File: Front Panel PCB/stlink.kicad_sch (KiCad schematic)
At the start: 22 parts, among them J3 LCD I2C, J4 Fan Tach and PWM, J5 Fan Power and GND, J6 VP and VN, J7 DEBUG, Q21 2N3904, SW1 SW_Push, U12 STM32G031K8Tx

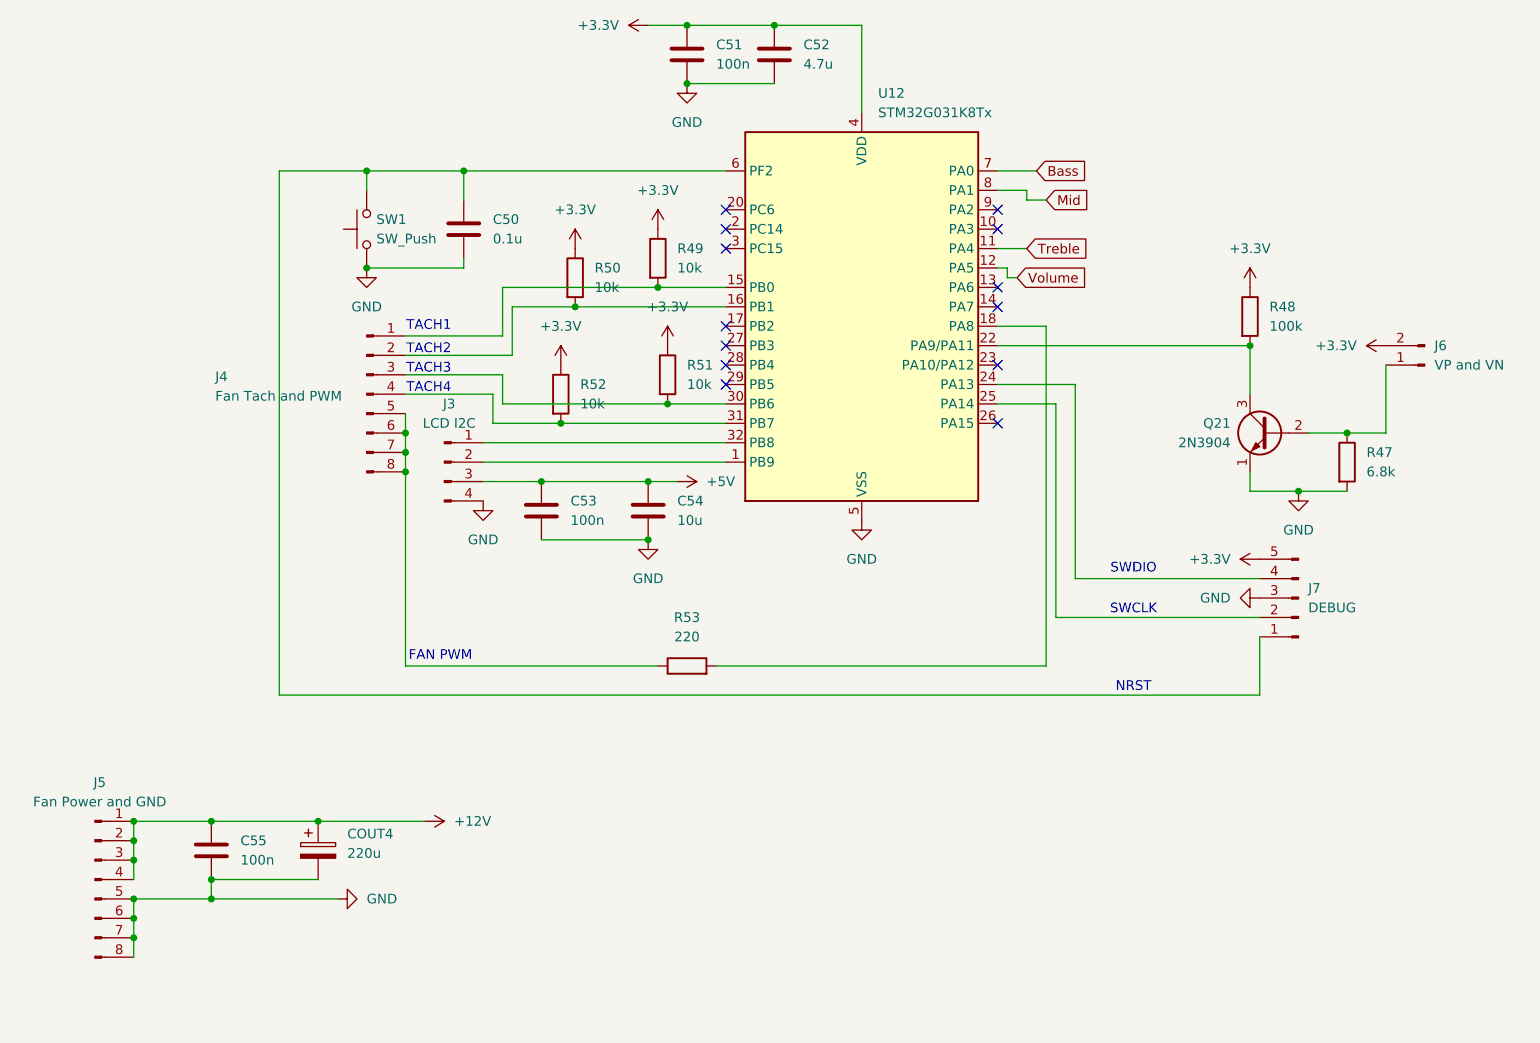
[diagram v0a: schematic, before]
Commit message: Checked ERC, assigned all footprints, time to start PCB design, will start with the equiliser
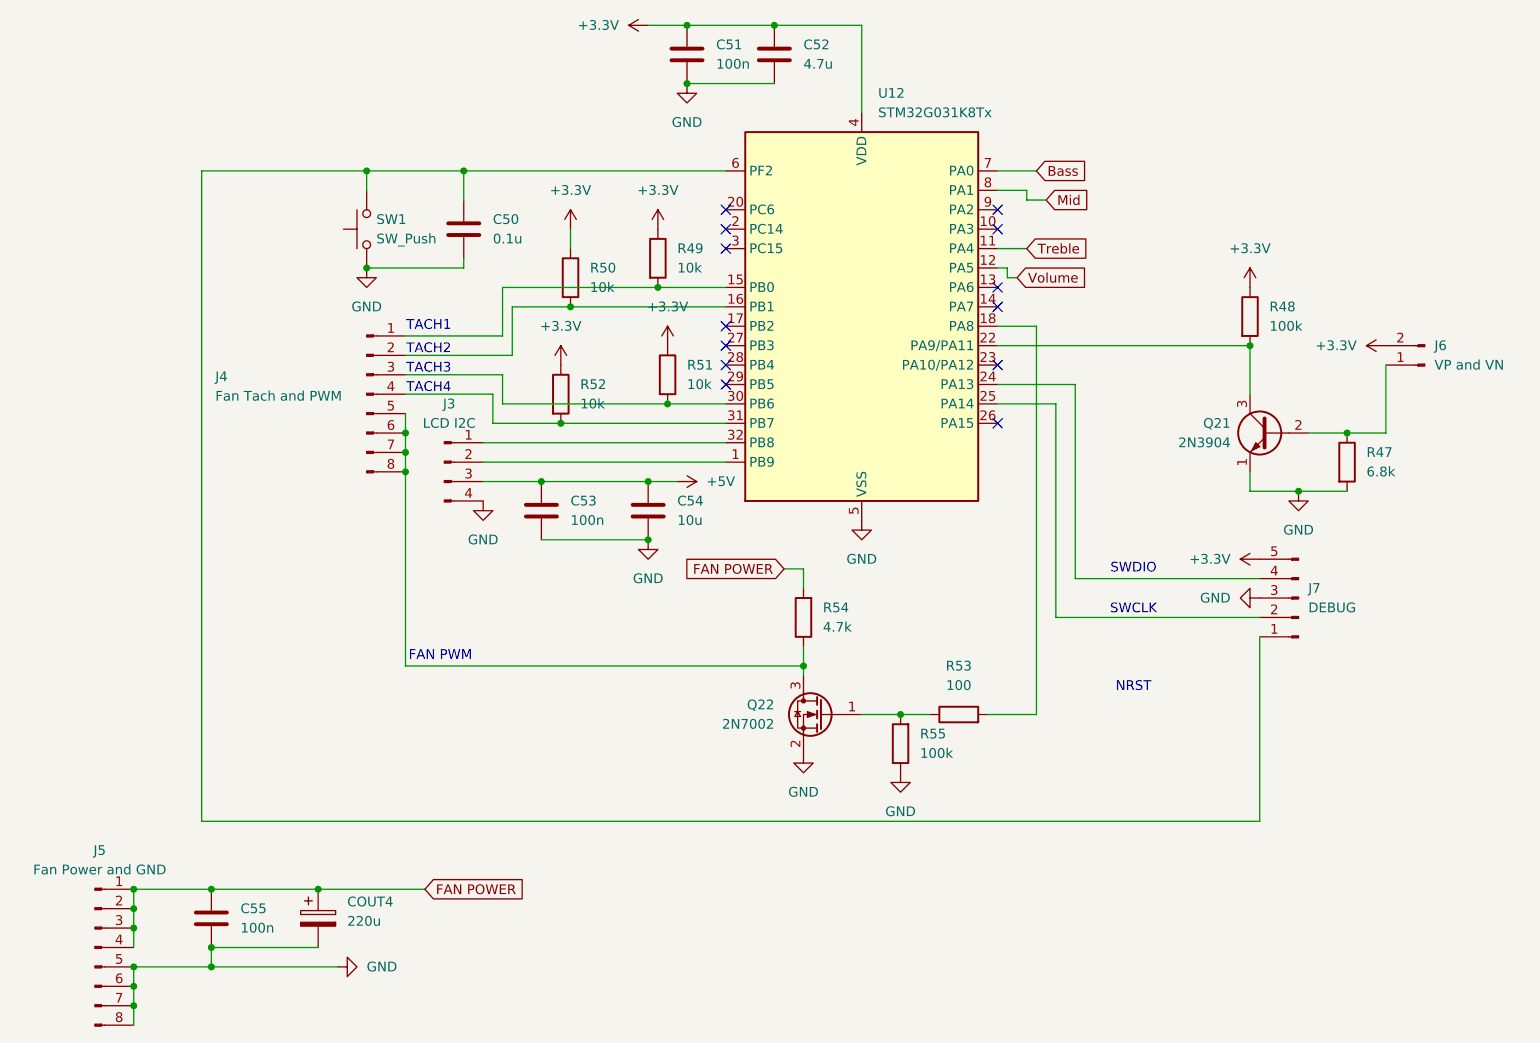
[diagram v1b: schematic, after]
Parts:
- added Q22: 2N7002, Package_TO_SOT_SMD:SOT-23, symbol Transistor_FET:2N7002
- added R54: 4.7k, Resistor_THT:R_Axial_DIN0207_L6.3mm_D2.5mm_P10.16mm_Horizontal, symbol Device:R
- added R55: 100k, Resistor_THT:R_Axial_DIN0207_L6.3mm_D2.5mm_P10.16mm_Horizontal, symbol Device:R
- C50, C51, C53, C55: footprint (none) -> Capacitor_THT:C_Rect_L7.2mm_W2.5mm_P5.00mm
- C52: footprint (none) -> GCJ31CC71H475KA01L:CAPC3216X190N
- C54: footprint (none) -> GCM32EC71H106KA03L:CAP_GCM32_MUR
- COUT4: footprint (none) -> Capacitor_THT:CP_Radial_D6.3mm_P2.50mm
- J3: footprint (none) -> Connector_PinHeader_2.00mm:PinHeader_1x04_P2.00mm_Vertical
- J4: footprint (none) -> Connector_JST:JST_XH_B8B-XH-A_1x08_P2.50mm_Vertical
- J5: footprint (none) -> Connector_Molex:Molex_Micro-Fit_3.0_43045-0812_2x04_P3.00mm_Vertical
- J6: footprint (none) -> Connector_JST:JST_PH_B2B-PH-K_1x02_P2.00mm_Vertical
- J7: footprint (none) -> Connector_JST:JST_PH_B5B-PH-K_1x05_P2.00mm_Vertical
- R47, R48, R49, R50, R51, R52: footprint (none) -> Resistor_THT:R_Axial_DIN0207_L6.3mm_D2.5mm_P10.16mm_Horizontal
- R53: value 220 -> 100; footprint (none) -> Resistor_THT:R_Axial_DIN0207_L6.3mm_D2.5mm_P10.16mm_Horizontal
- SW1: footprint (none) -> Button_Switch_THT:SW_PUSH_6mm_H5mm
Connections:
- net GND: now also Q22.2 (S), R55.1
- net at J4.5 (Pin_5), J4.6 (Pin_6), J4.7 (Pin_7)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: now also Q22.3 (D), R54.1; no longer R53.1
- net +12V renamed FAN POWER
- net FAN POWER: now also R54.2
- new net: Q22.1 (G), R53.1, R55.2
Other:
- moved on the sheet: C55, COUT4, J5, R50

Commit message: Hierarichal sheets and started PCB design
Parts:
- removed C50: 0.1u, Capacitor_THT:C_Rect_L7.2mm_W2.5mm_P5.00mm, symbol Device:C
- removed C51, C53, C55: 100n, Capacitor_THT:C_Rect_L7.2mm_W2.5mm_P5.00mm, symbol Device:C
- removed C52: 4.7u, GCJ31CC71H475KA01L:CAPC3216X190N, symbol Device:C
- removed C54: 10u, GCM32EC71H106KA03L:CAP_GCM32_MUR, symbol Device:C
- removed COUT4: 220u, Capacitor_THT:CP_Radial_D6.3mm_P2.50mm, symbol Device:C_Polarized
- removed J3: LCD I2C, Connector_PinHeader_2.00mm:PinHeader_1x04_P2.00mm_Vertical, symbol Connector:Conn_01x04_Pin
- removed J4: Fan Tach and PWM, Connector_JST:JST_XH_B8B-XH-A_1x08_P2.50mm_Vertical, symbol Connector:Conn_01x08_Pin
- removed J5: Fan Power and GND, Connector_Molex:Molex_Micro-Fit_3.0_43045-0812_2x04_P3.00mm_Vertical, symbol Connector:Conn_01x08_Pin
- removed J6: VP and VN, Connector_JST:JST_PH_B2B-PH-K_1x02_P2.00mm_Vertical, symbol Connector:Conn_01x02_Pin
- removed J7: DEBUG, Connector_JST:JST_PH_B5B-PH-K_1x05_P2.00mm_Vertical, symbol Connector:Conn_01x05_Pin
- removed Q21: 2N3904, Package_TO_SOT_THT:TO-92_Inline, symbol Transistor_BJT:2N3904
- removed Q22: 2N7002, Package_TO_SOT_SMD:SOT-23, symbol Transistor_FET:2N7002
- removed R47: 6.8k, Resistor_THT:R_Axial_DIN0207_L6.3mm_D2.5mm_P10.16mm_Horizontal, symbol Device:R
- removed R48, R55: 100k, Resistor_THT:R_Axial_DIN0207_L6.3mm_D2.5mm_P10.16mm_Horizontal, symbol Device:R
- removed R49, R50, R51, R52: 10k, Resistor_THT:R_Axial_DIN0207_L6.3mm_D2.5mm_P10.16mm_Horizontal, symbol Device:R
- removed R53: 100, Resistor_THT:R_Axial_DIN0207_L6.3mm_D2.5mm_P10.16mm_Horizontal, symbol Device:R
- removed R54: 4.7k, Resistor_THT:R_Axial_DIN0207_L6.3mm_D2.5mm_P10.16mm_Horizontal, symbol Device:R
- removed SW1: SW_Push, Button_Switch_THT:SW_PUSH_6mm_H5mm, symbol Switch:SW_Push
- removed U12: STM32G031K8Tx, Package_QFP:LQFP-32_7x7mm_P0.8mm, symbol MCU_ST_STM32G0:STM32G031K8Tx
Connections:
- no-connect marks 13 -> 0
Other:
- note removed: "FAN PWM"
- note removed: "NRST"
- note removed: "SWCLK"
- note removed: "SWDIO"
- note removed: "TACH1"
- note removed: "TACH2"
- note removed: "TACH3"
- note removed: "TACH4"
